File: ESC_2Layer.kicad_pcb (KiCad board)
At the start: 2 copper layers, 50 x 35 mm, 80 parts, among them J1 SWD, Q1 PSMN011-30YLC, Q2 PSMN011-30YLC, Q3 PSMN011-30YLC, Q4 PSMN011-30YLC, Q5 PSMN011-30YLC, Q6 PSMN011-30YLC, U1 MIC4604, U2 MIC4604, U3 MIC4604, U4 STM32F030K6Tx, U5 AP1117-33

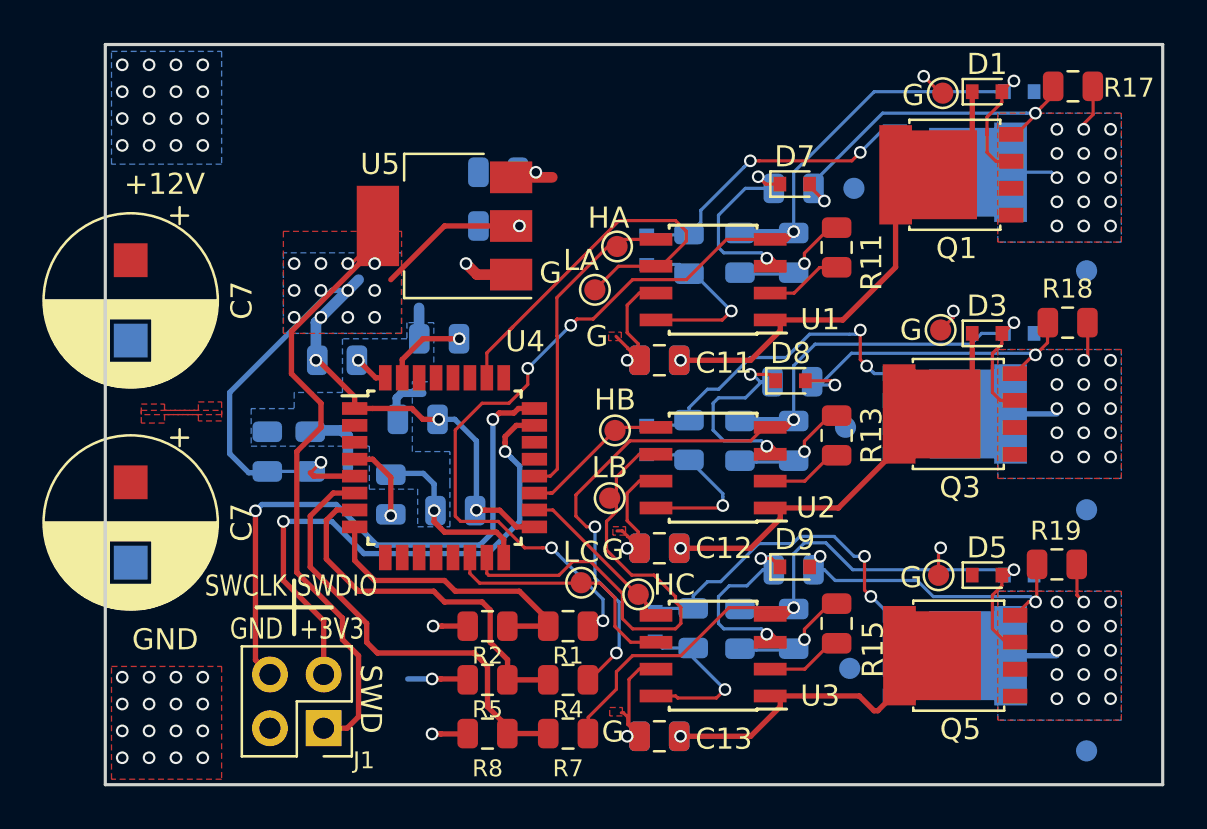
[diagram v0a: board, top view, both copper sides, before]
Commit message: Added PWM input
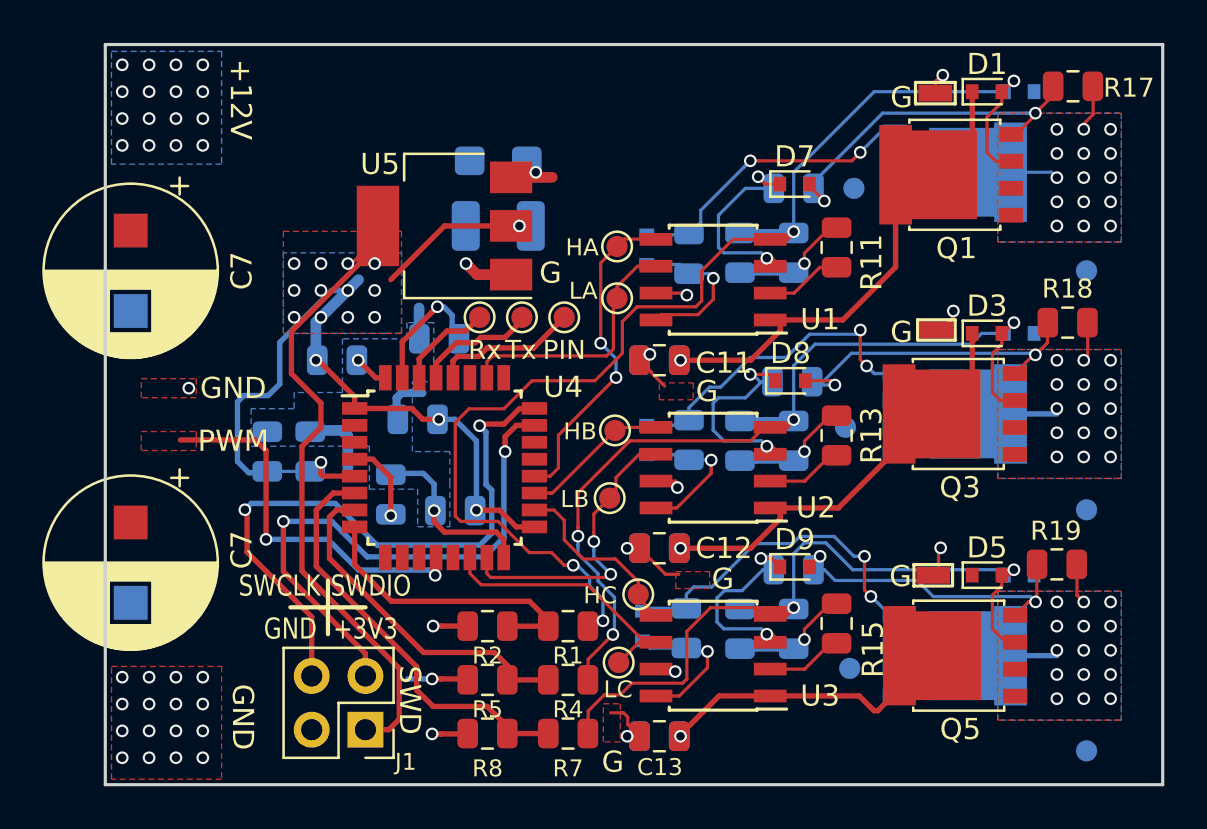
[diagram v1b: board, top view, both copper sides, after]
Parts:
- removed G: Q3_G, TestPoint:TestPoint_Pad_D1.0mm
- removed LA: LA, TestPoint:TestPoint_Pad_D1.0mm
- removed LC: LC, TestPoint:TestPoint_Pad_D1.0mm
- added TP1: Q3_G, TestPoint:TestPoint_Pad_D1.0mm, F.Cu at (89.2, 62.3)
- added TP13: LA, TestPoint:TestPoint_Pad_D1.0mm, F.Cu at (67.7, 72.9)
- added TP13: LA, TestPoint:TestPoint_Pad_D1.0mm, F.Cu at (69.7, 72.9)
- added TP13: LA, TestPoint:TestPoint_Pad_D1.0mm, F.Cu at (71.7, 72.9)
- added TP13: LA, TestPoint:TestPoint_Pad_D1.0mm, F.Cu at (74.2, 72.0)
- added TP15: LC, TestPoint:TestPoint_Pad_D1.0mm, F.Cu at (74.3, 89.2)
- C14: footprint Capacitor_SMD:C_0805_2012Metric -> Capacitor_Tantalum_SMD:CP_EIA-3216-18_Kemet-A
- C18: footprint Capacitor_SMD:C_0805_2012Metric -> Capacitor_Tantalum_SMD:CP_EIA-3528-15_AVX-H
- moved J1 1.98 mm to (62.3, 92.4)
- moved C7 1.90 mm to (51.2, 82.6)
- moved C7 1.40 mm to (51.2, 68.8)
- moved D11 0.60 mm to (75.4, 87.5)
- moved C14 0.54 mm to (68.6, 65.5)
- moved R22 0.33 mm to (77.5, 87.6)
- moved TP5 0.25 mm to (89.2, 85.1)
- moved TP3 0.20 mm to (89.3, 73.5)
- renumbered HA to TP10, HB to TP11, HC to TP12, LB to TP14, G to TP2, G to TP3, G to TP4, G to TP5, G to TP6, G to TP7, G to TP8, G to TP9
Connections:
- U4 pad 10: (no net) -> Net-(U4-Pad10)
- U4 pad 11: (no net) -> Net-(U4-Pad11)
- U4 pad 12: (no net) -> /PWM_IN
- U4 pad 13: (no net) -> Net-(U4-Pad13)
- U4 pad 2: (no net) -> Net-(U4-Pad2)
- U4 pad 21: (no net) -> Net-(U4-Pad21)
- U4 pad 22: (no net) -> Net-(U4-Pad22)
- U4 pad 25: (no net) -> Net-(U4-Pad25)
- U4 pad 27: (no net) -> Net-(U4-Pad27)
- U4 pad 28: (no net) -> /DBG_PIN
- U4 pad 29: (no net) -> /UART1_TX
- U4 pad 3: (no net) -> Net-(U4-Pad3)
- U4 pad 30: (no net) -> /UART1_RX
- U4 pad 9: (no net) -> Net-(U4-Pad9)
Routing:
- net /PWM_IN: track 0.00 -> 18.0 mm, vias 0 -> 2
- net /LOW_B: track 23.9 -> 14.0 mm, vias 0 -> 2
- net /DBG_PIN: track 0.00 -> 6.91 mm
- net /LOW_A: track 19.8 -> 12.9 mm
- net GND: track 49.0 -> 42.6 mm, vias 28 -> 32
- net /UART1_TX: track 0.00 -> 5.74 mm
- net /UART1_RX: track 0.00 -> 4.57 mm
- net /SWCLK: track 27.9 -> 30.3 mm
- net /BOOT0: track 3.97 -> 6.16 mm
- net /OUT_A: track 64.7 -> 66.4 mm, vias 21 -> 19
- net /BEMF_C: track 21.3 -> 19.9 mm
- net /LOW_C: track 11.2 -> 12.6 mm
- net /BEMF_B: track 17.7 -> 16.4 mm
- net /HIGH_C: track 7.68 -> 8.80 mm
- net Net-(D12-Pad1): track 8.65 -> 7.53 mm
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- added copper zone on F.Cu, net /PWM_IN
- removed copper zone on F.Cu, net (none)
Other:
- board text added: "HA"
- board text added: "HB"
- board text added: "HC"
- board text added: "LA"
- board text added: "LB"
- board text added: "LC"
- board text added: "PIN"
- board text added: "PWM"
- board text added: "Rx"
- board text added: "Tx"
